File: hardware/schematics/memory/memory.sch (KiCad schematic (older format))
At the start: 5 parts

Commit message: I started working on the PCBs
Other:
- moved on the sheet: C?, J?, U?

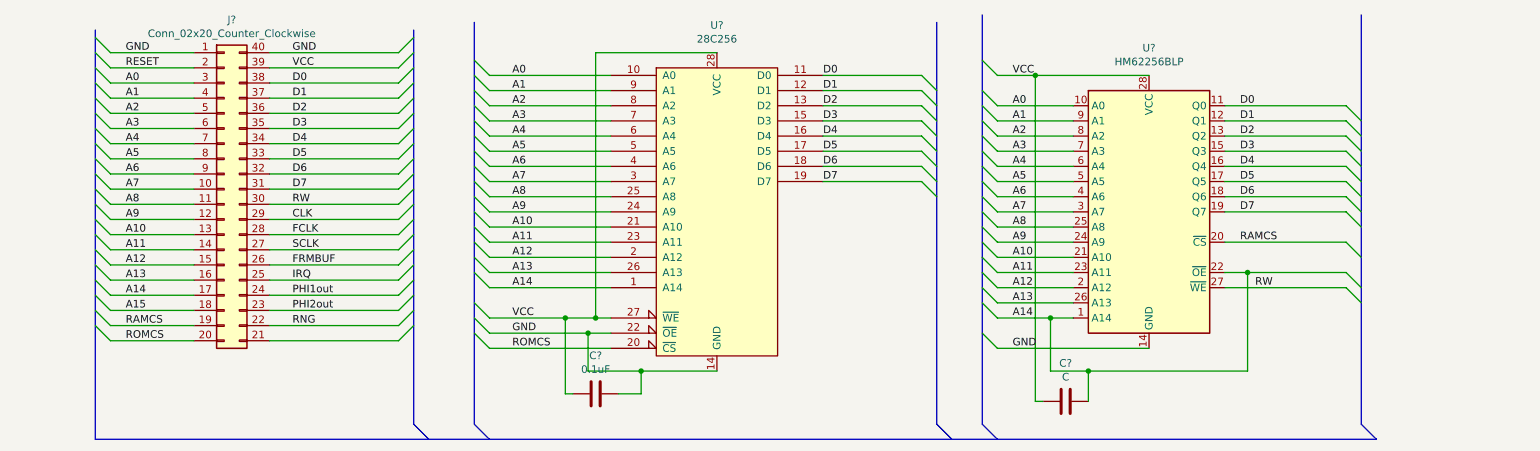
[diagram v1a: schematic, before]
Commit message: I ordered the PCB from jlcpcb
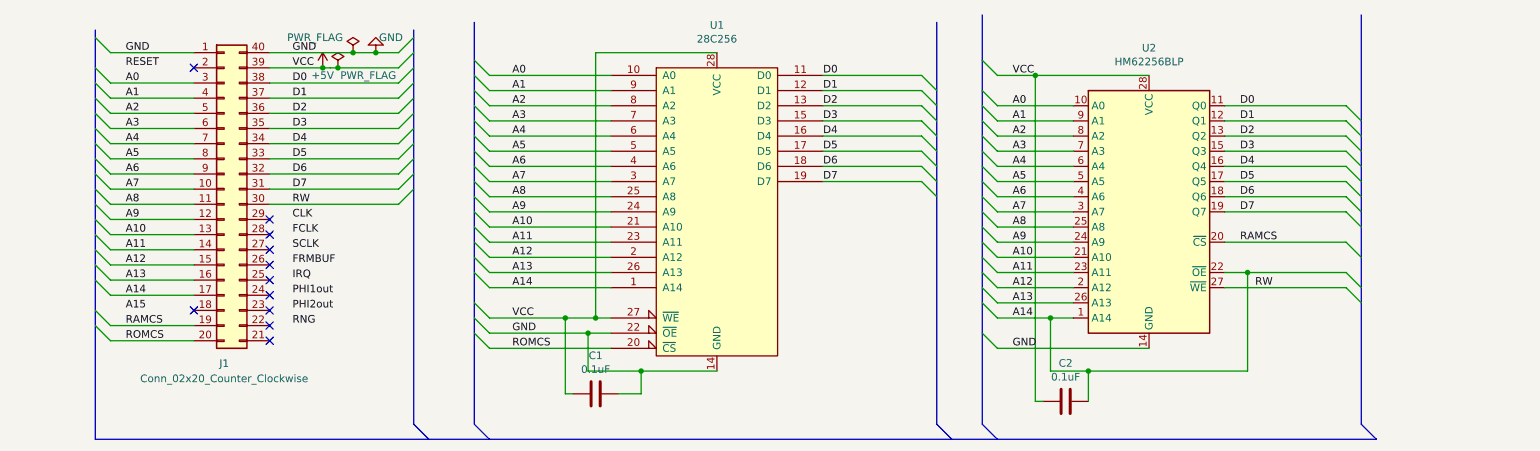
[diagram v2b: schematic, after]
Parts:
- C1: renamed from C?; footprint (none) -> Capacitor_THT:C_Disc_D3.8mm_W2.6mm_P2.50mm
- C2: renamed from C?; value C -> 0.1uF; footprint (none) -> Capacitor_THT:C_Disc_D3.8mm_W2.6mm_P2.50mm
- J1: renamed from J?; footprint (none) -> m6502:PinHeader_2x20_P2.54mm_Horizontal_Counter_Clockwise
- U1: renamed from U?; footprint (none) -> Package_DIP:DIP-28_W15.24mm_Socket
- U2: renamed from U?; footprint Package_DIP:DIP-28_W15.24mm -> Package_DIP:DIP-28_W15.24mm_Socket
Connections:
- net A15: no longer J1.18 (Pin_18)
- net CLK: no longer J1.29 (Pin_29)
- net FCLK: no longer J1.28 (Pin_28)
- net FRMBUF: no longer J1.26 (Pin_26)
- net IRQ: no longer J1.25 (Pin_25)
- net PHI1out: no longer J1.24 (Pin_24)
- net PHI2out: no longer J1.23 (Pin_23)
- net RESET: no longer J1.2 (Pin_2)
- net RNG: no longer J1.22 (Pin_22)
- net SCLK: no longer J1.27 (Pin_27)
- net VCC renamed +5V
- no-connect marks 0 -> 11
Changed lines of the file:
@@
 $EndDescr
 $Comp
-L 28c256:28C256 U?
+L 28c256:28C256 U1
 U 1 1 63387EE1
 P 5350 3500
-F 0 "U?" H 5350 4731 50  0000 C CNN
+F 0 "U1" H 5350 4731 50  0000 C CNN
 F 1 "28C256" H 5350 4640 50  0000 C CNN
-F 2 "" H 5350 3500 50  0001 C CNN
+F 2 "Package_DIP:DIP-28_W15.24mm_Socket" H 5350 3500 50  0001 C CNN
 F 3 "memory/28c256.pdf" H 5350 3500 50  0001 C CNN
 	1    5350 3500
@@
 $EndComp
 $Comp
-L Memory_RAM:HM62256BLP U?
+L Memory_RAM:HM62256BLP U2
 U 1 1 6338947A
 P 8200 3500
-F 0 "U?" H 8200 4581 50  0000 C CNN
+F 0 "U2" H 8200 4581 50  0000 C CNN
 F 1 "HM62256BLP" H 8200 4490 50  0000 C CNN
-F 2 "Package_DIP:DIP-28_W15.24mm" H 8200 3400 50  0001 C CNN
+F 2 "Package_DIP:DIP-28_W15.24mm_Socket" H 8200 3400 50  0001 C CNN
 F 3 "https://web.mit.edu/6.115/www/document/62256.pdf" H 8200 3400 50  0001 C CNN
 	1    8200 3500
@@
 $EndComp
 $Comp
-L Connector_Generic:Conn_02x20_Counter_Clockwise J?
+L Connector_Generic:Conn_02x20_Counter_Clockwise J1
 U 1 1 63389FA6
 P 2100 3350
-F 0 "J?" H 2150 4467 50  0000 C CNN
-F 1 "Conn_02x20_Counter_Clockwise" H 2150 4376 50  0000 C CNN
-F 2 "" H 2100 3350 50  0001 C CNN
+F 0 "J1" H 2100 2200 50  0000 C CNN
+F 1 "Conn_02x20_Counter_Clockwise" H 2100 2100 50  0000 C CNN
+F 2 "m6502:PinHeader_2x20_P2.54mm_Horizontal_Counter_Clockwise" H 2100 3350 50  0001 C CNN
 F 3 "~" H 2100 3350 50  0001 C CNN
 	1    2100 3350
@@
 	1250 2350 1350 2450
 Entry Wire Line
-	1250 2450 1350 2550
-Entry Wire Line
 	1250 2550 1350 2650
 Entry Wire Line
@@
 	1250 3950 1350 4050
 Entry Wire Line
-	1250 4050 1350 4150
-Entry Wire Line
 	1250 4150 1350 4250
 Entry Wire Line
@@
 	1350 2450 1900 2450
 Wire Wire Line
-	1350 2550 1900 2550
-Wire Wire Line
 	1350 2650 1900 2650
 Wire Wire Line
@@
 	1350 4050 1900 4050
 Wire Wire Line
-	1350 4150 1900 4150
-Wire Wire Line
 	1350 4250 1900 4250
 Wire Wire Line
@@
 	3250 2450 3350 2350
 Wire Wire Line
-	2400 2450 3250 2450
+	2400 2450 2950 2450
 Entry Wire Line
 	3250 2550 3350 2450
 Wire Wire Line
-	2400 2550 3250 2550
+	2400 2550 2800 2550
 Entry Wire Line
 	3250 2650 3350 2550
@@
 Wire Wire Line
 	2400 3450 3250 3450
-Entry Wire Line
-	3250 3550 3350 3450
-Wire Wire Line
-	2400 3550 3250 3550
-Entry Wire Line
-	3250 3650 3350 3550
-Wire Wire Line
-	2400 3650 3250 3650
-Entry Wire Line
-	3250 3750 3350 3650
-Wire Wire Line
-	2400 3750 3250 3750
-Entry Wire Line
-	3250 3850 3350 3750
-Wire Wire Line
-	2400 3850 3250 3850
-Entry Wire Line
-	3250 3950 3350 3850
-Wire Wire Line
-	2400 3950 3250 3950
-Entry Wire Line
-	3250 4050 3350 3950
-Wire Wire Line
-	2400 4050 3250 4050
-Entry Wire Line
-	3250 4150 3350 4050
-Wire Wire Line
-	2400 4150 3250 4150
-Entry Wire Line
-	3250 4250 3350 4150
-Wire Wire Line
-	2400 4250 3250 4250
-Entry Wire Line
-	3250 4350 3350 4250
-Wire Wire Line
-	2400 4350 3250 4350
 Text Label 1450 2450 0    50   ~ 0
 GND
@@
 VCC
 $Comp
-L Device:C C?
+L Device:C C1
 U 1 1 63501102
 P 4550 4700
-F 0 "C?" V 4298 4700 50  0000 C CNN
+F 0 "C1" V 4298 4700 50  0000 C CNN
 F 1 "0.1uF" V 4389 4700 50  0000 C CNN
-F 2 "" H 4588 4550 50  0001 C CNN
+F 2 "Capacitor_THT:C_Disc_D3.8mm_W2.6mm_P2.50mm" H 4588 4550 50  0001 C CNN
 F 3 "~" H 4550 4700 50  0001 C CNN
 	1    4550 4700
@@
 	4850 4550 5350 4550
 $Comp
-L Device:C C?
+L Device:C C2
 U 1 1 6350C827
 P 7650 4750
-F 0 "C?" V 7398 4750 50  0000 C CNN
-F 1 "C" V 7489 4750 50  0000 C CNN
-F 2 "" H 7688 4600 50  0001 C CNN
+F 0 "C2" V 7398 4750 50  0000 C CNN
+F 1 "0.1uF" V 7489 4750 50  0000 C CNN
+F 2 "Capacitor_THT:C_Disc_D3.8mm_W2.6mm_P2.50mm" H 7688 4600 50  0001 C CNN
 F 3 "~" H 7650 4750 50  0001 C CNN
 	1    7650 4750
@@
 Wire Wire Line
 	7800 4550 8850 4550
+$Comp
+L power:PWR_FLAG #FLG02
+U 1 1 633C0D61
+P 2950 2450
+F 0 "#FLG02" H 2950 2525 50  0001 C CNN
+F 1 "PWR_FLAG" H 2700 2550 50  0000 C CNN
+F 2 "" H 2950 2450 50  0001 C CNN
+F 3 "~" H 2950 2450 50  0001 C CNN
+	1    2950 2450
+	1    0    0    -1
+$EndComp
+Connection ~ 2950 2450
+Wire Wire Line
+	2950 2450 3100 2450
+$Comp
+L power:GND #PWR02
+U 1 1 633C1330
+P 3100 2450
+F 0 "#PWR02" H 3100 2200 50  0001 C CNN
+F 1 "GND" H 3000 2350 50  0000 C CNN
+F 2 "" H 3100 2450 50  0001 C CNN
+F 3 "" H 3100 2450 50  0001 C CNN
+	1    3100 2450
+	-1   0    0    1
+$EndComp
+Connection ~ 3100 2450
+Wire Wire Line
+	3100 2450 3250 2450
+$Comp
+L power:+5V #PWR01
+U 1 1 633C1B8D
+P 2750 2550
+F 0 "#PWR01" H 2750 2400 50  0001 C CNN
+F 1 "+5V" H 2750 2500 50  0000 C CNN
+F 2 "" H 2750 2550 50  0001 C CNN
+F 3 "" H 2750 2550 50  0001 C CNN
+	1    2750 2550
+	1    0    0    -1
+$EndComp
+Connection ~ 2750 2550
+Wire Wire Line
+	2800 2550 2850 2550
+NoConn ~ 2400 3550
+NoConn ~ 2400 3650
+NoConn ~ 2400 3750
+NoConn ~ 2400 3850
+NoConn ~ 2400 3950
+NoConn ~ 2400 4050
+NoConn ~ 2400 4150
+NoConn ~ 2400 4250
+NoConn ~ 2400 4350
+NoConn ~ 1900 4150
+NoConn ~ 1900 2550
 Wire Bus Line
 	1250 5000 9700 5000
+Wire Bus Line
+	3350 2300 3350 4900
 Wire Bus Line
 	6800 2250 6800 4900
@@
 	7100 2200 7100 4900
 Wire Bus Line
-	3350 2300 3350 4900
-Wire Bus Line
 	1250 2300 1250 5000
 Wire Bus Line
 	3750 2250 3750 4900
+$Comp
+L power:PWR_FLAG #FLG01
+U 1 1 6340AEA7
+P 2850 2550
+F 0 "#FLG01" H 2850 2625 50  0001 C CNN
+F 1 "PWR_FLAG" H 3050 2500 50  0000 C CNN
+F 2 "" H 2850 2550 50  0001 C CNN
+F 3 "~" H 2850 2550 50  0001 C CNN
+	1    2850 2550
+	1    0    0    -1
+$EndComp
+Connection ~ 2850 2550
+Wire Wire Line
+	2850 2550 3250 2550
 $EndSCHEMATC
